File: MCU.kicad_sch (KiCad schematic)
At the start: 31 parts, among them J10 SWD, J11 UART, J12 I2C1, Q16 AO3401A, Q17 2N7002W, U12 STM32F030C8Tx

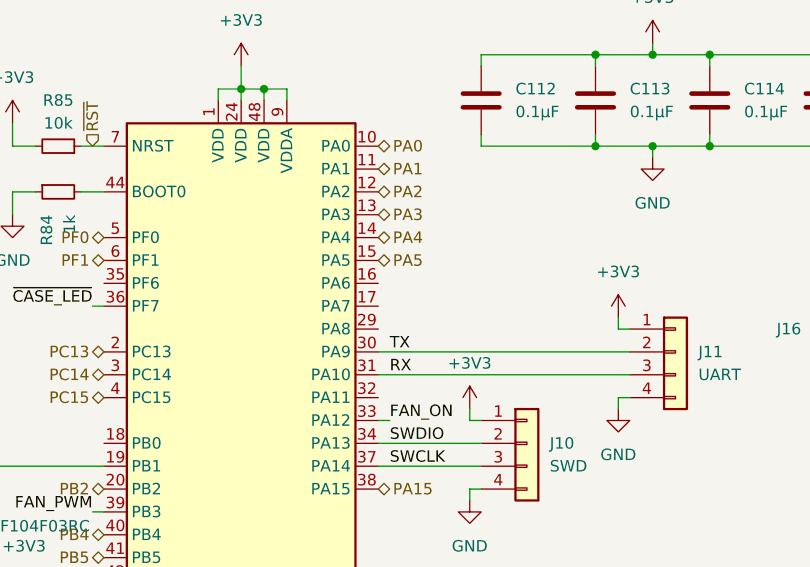
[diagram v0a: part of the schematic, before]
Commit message: added new links to mcu
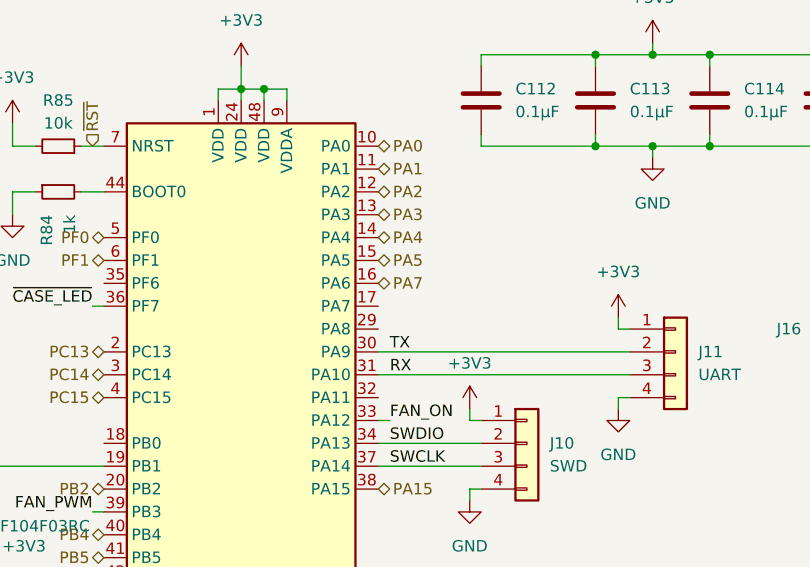
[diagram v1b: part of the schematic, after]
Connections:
- net PA7: now reaches U12.16 (PA6)
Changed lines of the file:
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@@
+		)
+	)
+	(hierarchical_label "PA7"
+		(shape bidirectional)
+		(at 71.12 55.88 0)
+		(effects
+			(font
+				(size 1.27 1.27)
+			)
+			(justify left)
 		)
 	)

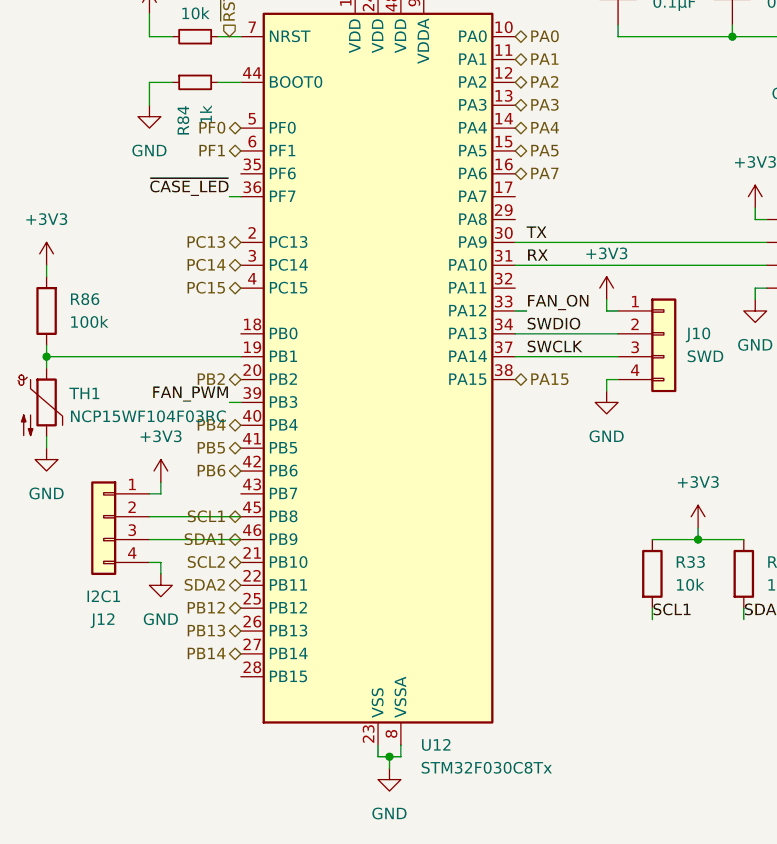
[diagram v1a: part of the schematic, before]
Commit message: added pd connected to mcu and the option to turn off
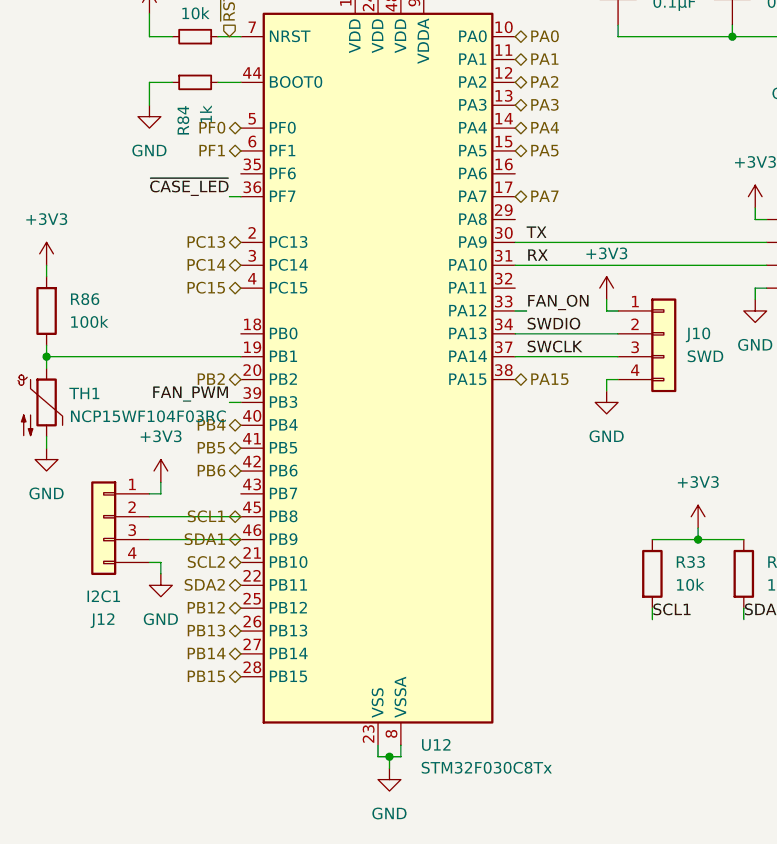
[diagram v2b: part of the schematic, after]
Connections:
- net PA7: now also U12.17 (PA7); no longer U12.16 (PA6)
- net PB15: now reaches U12.28 (PB15)
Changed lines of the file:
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@@
 		)
 	)
-	(hierarchical_label "PA7"
+	(hierarchical_label "PA5"
 		(shape bidirectional)
-		(at 71.12 55.88 0)
+		(at 71.12 53.34 0)
 		(effects
 			(font
@@
 		)
 	)
-	(hierarchical_label "PA5"
+	(hierarchical_label "PA7"
 		(shape bidirectional)
-		(at 71.12 53.34 0)
+		(at 71.12 58.42 0)
 		(effects
 			(font
@@
 		(effects
 			(font
+				(size 1.27 1.27)
+			)
+			(justify right)
+		)
+	)
+	(hierarchical_label "PB15"
+		(shape bidirectional)
+		(at 40.64 111.76 180)
+		(effects
+			(font

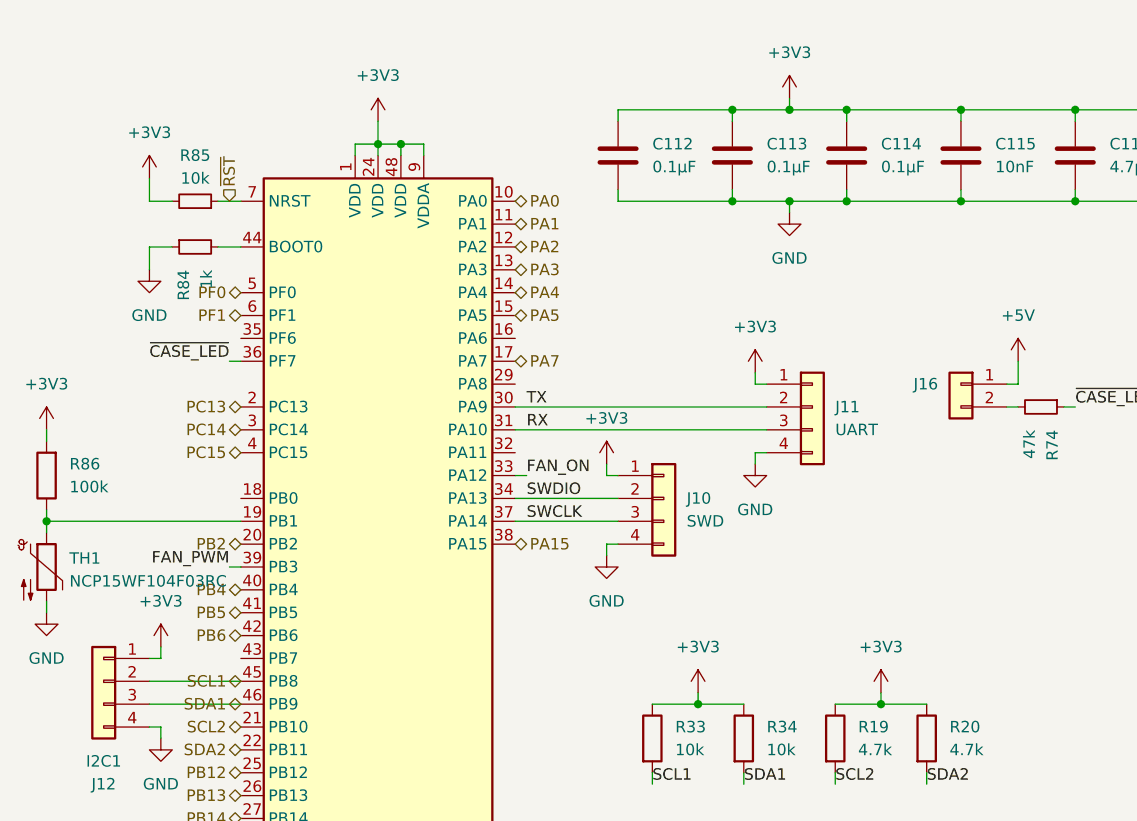
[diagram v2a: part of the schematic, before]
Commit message: added 3v3vsb to mcu
added 3v3vsb to mcu
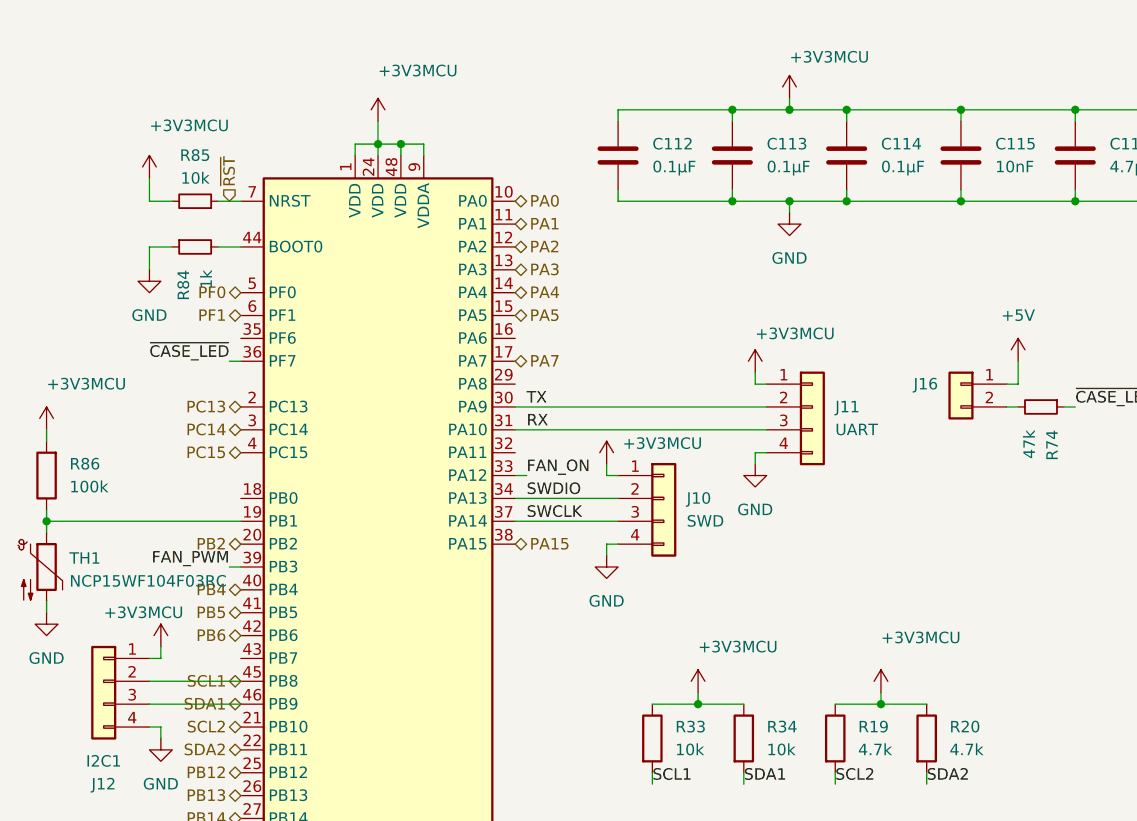
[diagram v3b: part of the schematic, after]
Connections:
- net +3V3 renamed +3V3MCU
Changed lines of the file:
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@@
 		(on_board yes)
 		(dnp no)
-		(fields_autoplaced yes)
 		(property "Reference" "#PWR0125"
 			(at 81.28 73.66 0)
@@
 			)
 		)
-		(property "Value" "+3V3"
-			(at 81.28 64.77 0)
+		(property "Value" "+3V3MCU"
+			(at 83.058 67.564 0)
 			(effects
 				(font
 					(size 1.27 1.27)
 				)
+				(justify left)
 			)
 		)
@@
 		(on_board yes)
 		(dnp no)
-		(fields_autoplaced yes)
 		(property "Reference" "#PWR0119"
 			(at 30.48 41.91 0)
@@
 			)
 		)
-		(property "Value" "+3V3"
-			(at 30.48 33.02 0)
+		(property "Value" "+3V3MCU"
+			(at 30.48 32.258 0)
 			(effects
 				(font
 					(size 1.27 1.27)
 				)
+				(justify left)
 			)
 		)
@@
 		(on_board yes)
 		(dnp no)
-		(fields_autoplaced yes)
 		(property "Reference" "#PWR0128"
 			(at 111.76 99.06 0)
@@
 			)
 		)
-		(property "Value" "+3V3"
-			(at 111.76 90.17 0)
+		(property "Value" "+3V3MCU"
+			(at 111.76 89.154 0)
 			(effects
 				(font
 					(size 1.27 1.27)
 				)
+				(justify left)
 			)
 		)
@@
 		(on_board yes)
 		(dnp no)
-		(fields_autoplaced yes)
 		(property "Reference" "#PWR0124"
 			(at 55.88 35.56 0)
@@
 			)
 		)
-		(property "Value" "+3V3"
-			(at 55.88 26.67 0)
+		(property "Value" "+3V3MCU"
+			(at 55.88 26.162 0)
 			(effects
 				(font
 					(size 1.27 1.27)
 				)
+				(justify left)
 			)
 		)
@@
 		(on_board yes)
 		(dnp no)
-		(fields_autoplaced yes)
 		(property "Reference" "#PWR067"
 			(at 91.44 99.06 0)
@@
 			)
 		)
-		(property "Value" "+3V3"
+		(property "Value" "+3V3MCU"
 			(at 91.44 90.17 0)
 			(effects
@@
 					(size 1.27 1.27)
 				)
+				(justify left)
 			)
 		)
@@
 		(on_board yes)
 		(dnp no)
-		(fields_autoplaced yes)
 		(property "Reference" "#PWR018"
 			(at 31.75 93.98 0)
@@
 			)
 		)
-		(property "Value" "+3V3"
-			(at 31.75 85.09 0)
+		(property "Value" "+3V3MCU"
+			(at 25.4 86.36 0)
 			(effects
 				(font
 					(size 1.27 1.27)
 				)
+				(justify right)
 			)
 		)
@@
 		(on_board yes)
 		(dnp no)
-		(fields_autoplaced yes)
 		(property "Reference" "#PWR01"
 			(at 97.79 63.5 0)
@@
 			)
 		)
-		(property "Value" "+3V3"
-			(at 97.79 54.61 0)
+		(property "Value" "+3V3MCU"
+			(at 97.79 55.372 0)
 			(effects
 				(font
 					(size 1.27 1.27)
 				)
+				(justify left)
 			)
 		)
@@
 		(on_board yes)
 		(dnp no)
-		(fields_autoplaced yes)
 		(property "Reference" "#PWR068"
 			(at 19.05 69.85 0)
@@
 			)
 		)
-		(property "Value" "+3V3"
+		(property "Value" "+3V3MCU"
 			(at 19.05 60.96 0)
 			(effects
@@
 					(size 1.27 1.27)
 				)
+				(justify left)
 			)
 		)
@@
 		(on_board yes)
 		(dnp no)
-		(fields_autoplaced yes)
 		(property "Reference" "#PWR0123"
 			(at 101.6 33.02 0)
@@
 			)
 		)
-		(property "Value" "+3V3"
-			(at 101.6 24.13 0)
+		(property "Value" "+3V3MCU"
+			(at 101.6 24.638 0)
 			(effects
 				(font
 					(size 1.27 1.27)
 				)
+				(justify left)
 			)
 		)
